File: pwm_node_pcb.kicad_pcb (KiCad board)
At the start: 4 copper layers, 40 x 35 mm, 42 parts, among them J1 CAN1, J2 TC2050-IDC-NL, J3 Battery, J5 Load Source, J6 5V Breakout, U1 LMR51430, U2 TJA1051T/3, U3 LD1117S33CTR, U4 STM32L432KCU, U5 TXB0104QPWRQ1, Y1 ECS-2520MV-080-BN

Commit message: Add version silkscreen and update pictures
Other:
- board text added: "Daniel Jeon pwm_node_pcb v0.1.0-alpha"
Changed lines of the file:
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@@
+		)
+	)
+	(gr_text "Daniel Jeon\npwm_node_pcb\nv0.1.0-alpha"
+		(at 165.5 97 0)
+		(layer "B.SilkS")
+		(effects
+			(font
+				(size 1 1)
+				(thickness 0.2)
+				(bold yes)
+			)
+			(justify top mirror)
 		)
 	)

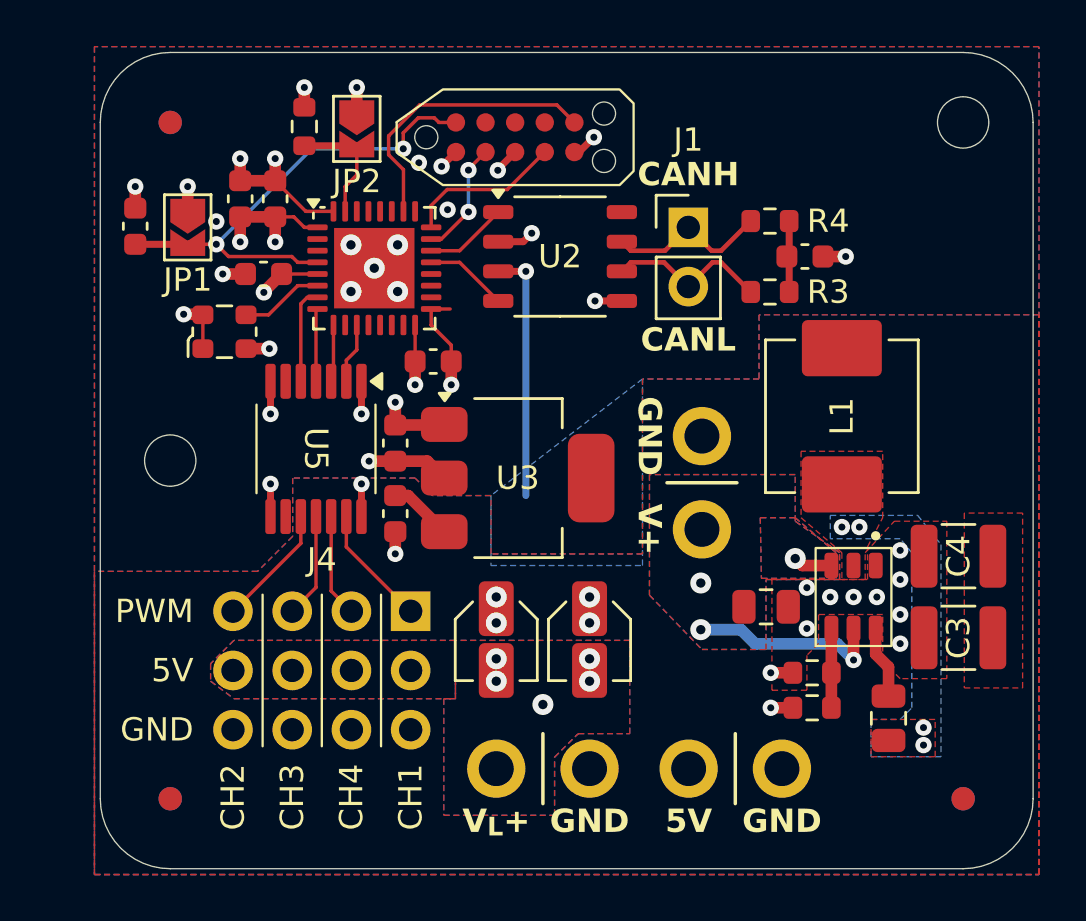
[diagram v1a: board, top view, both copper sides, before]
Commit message: Add minor decoupling caps, board cleanup
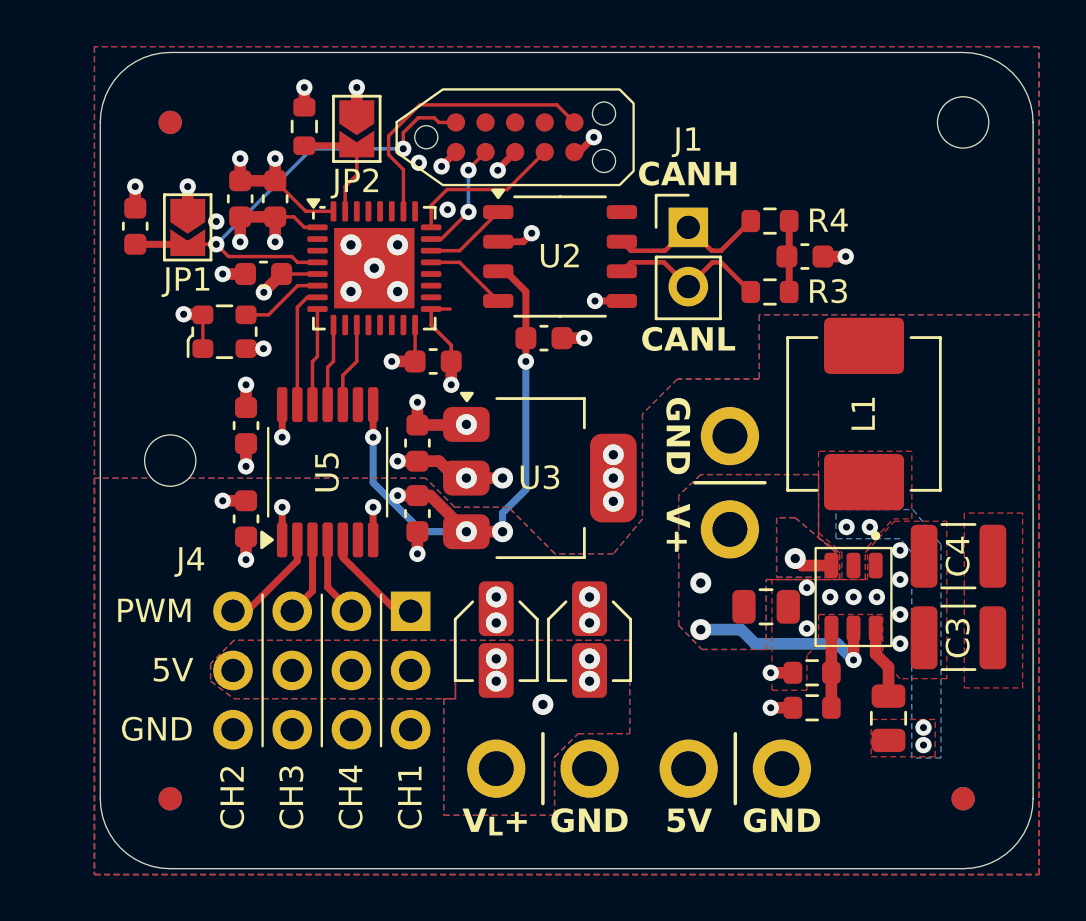
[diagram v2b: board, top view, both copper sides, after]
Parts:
- added C16: 100n, Capacitor_SMD:C_0603_1608Metric, F.Cu at (143.0, 115.8)
- added C17: 100n, Capacitor_SMD:C_0603_1608Metric, F.Cu at (143.0, 111.8)
- added C27: 100n, Capacitor_SMD:C_0603_1608Metric, F.Cu at (155.8, 108.0)
- moved J3 1.20 mm to (163.8, 114.2)
- moved U5 1.12 mm to (146.5, 113.8), turned to 90 degrees
- moved L1 0.96 mm to (169.5, 111.2)
- moved C5 0.95 mm to (150.3, 115.5)
- moved C6 0.95 mm to (150.3, 112.5)
- moved U3 0.95 mm to (155.6, 114.0)
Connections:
- U5 pad 1: +3V3 -> +5V
- U5 pad 10: /PWM2_{5V} -> /TIM1_CH1
- U5 pad 11: /PWM3_{5V} -> /TIM1_CH4
- U5 pad 12: /PWM4_{5V} -> /TIM1_CH3
- U5 pad 13: /PWM1_{5V} -> /TIM1_CH2
- U5 pad 14: +5V -> +3V3
- U5 pad 2: /TIM1_CH1 -> /PWM2_{5V}
- U5 pad 3: /TIM1_CH4 -> /PWM3_{5V}
- U5 pad 4: /TIM1_CH3 -> /PWM4_{5V}
- U5 pad 5: /TIM1_CH2 -> /PWM1_{5V}
- U5 pad 8: +3V3 -> +5V
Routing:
- net +5V: track 15.9 -> 29.4 mm, vias 3 -> 8
- net GND: track 24.9 -> 27.6 mm, vias 37 -> 41
- net /TIM1_CH1: track 2.60 -> 3.66 mm
- net /TIM1_CH2: track 4.15 -> 5.21 mm
- net /TIM1_CH3: track 3.13 -> 4.19 mm
- net /TIM1_CH4: track 2.45 -> 3.52 mm
- net /PWM3_{5V}: track 4.48 -> 3.42 mm
- net /PWM4_{5V}: track 4.42 -> 3.48 mm
- net +3V3: track 24.4 -> 25.2 mm, vias 11 -> 16
- net /PWM2_{5V}: track 5.27 -> 4.55 mm
- net /PWM1_{5V}: track 5.20 -> 4.62 mm

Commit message: Trace cleanup
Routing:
- net +5V: track 29.4 -> 25.8 mm
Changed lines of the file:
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@@
-	)
-	(segment
-		(start 154.885 103.865)
-		(end 153.815 103.865)
-		(width 0.3)
-		(layer "F.Cu")
-		(net 1)
 	)
 	(segment
@@
 	)
 	(segment
-		(start 155.25 103.5)
-		(end 154.885 103.865)
-		(width 0.3)
-		(layer "F.Cu")
-		(net 1)
-	)
-	(segment
 		(start 144.25 101.25)
 		(end 144.25 100.3)
@@
 	)
 	(segment
+		(start 155 103.865)
+		(end 153.815 103.865)
+		(width 0.3)
+		(layer "F.Cu")
+		(net 1)
+	)
+	(segment
 		(start 143.75 108.45)
 		(end 143 108.45)
@@
 	)
 	(via
-		(at 155.25 103.5)
+		(at 155 103.865)
 		(size 0.7)
 		(drill 0.3)
@@
 	)
 	(segment
+		(start 149.5 114.75)
+		(end 149 114.75)
+		(width 0.3)
+		(layer "B.Cu")
+		(net 2)
+	)
+	(segment
 		(start 154 115.5)
 		(end 154 116.3)
@@
 	)
 	(segment
-		(start 150.55 116.3)
-		(end 148.45 114.2)
-		(width 0.3)
-		(layer "B.Cu")
-		(net 2)
-	)
-	(segment
-		(start 152.45 116.3)
-		(end 150.55 116.3)
-		(width 0.3)
-		(layer "B.Cu")
-		(net 2)
-	)
-	(segment
 		(start 148.45 114.2)
 		(end 148.45 112.25)
+		(width 0.3)
+		(layer "B.Cu")
+		(net 2)
+	)
+	(segment
+		(start 149 114.75)
+		(end 148.45 114.2)
 		(width 0.3)
 		(layer "B.Cu")
@@
 		(polygon
 			(pts
-				(xy 152.5 104.25) (xy 152.5 104.75) (xy 153 104.75) (xy 152.965 104.25)
+				(xy 152.5 104.25) (xy 152.5 104.75) (xy 153 104.75) (xy 153 104.25)
 			)
 		)
@@
 		(polygon
 			(pts
-				(xy 151.98 123.46) (xy 151.48 123.46) (xy 151.48 128.46) (xy 156.23 128.46) (xy 156.23 125.964951)
+				(xy 151.98 123.46) (xy 151.48 123.46) (xy 151.48 128.71) (xy 156.23 128.71) (xy 156.23 125.964951)
 				(xy 157.245 124.96) (xy 159.455 124.96) (xy 159.455 120.96) (xy 151.98 120.96)
 			)

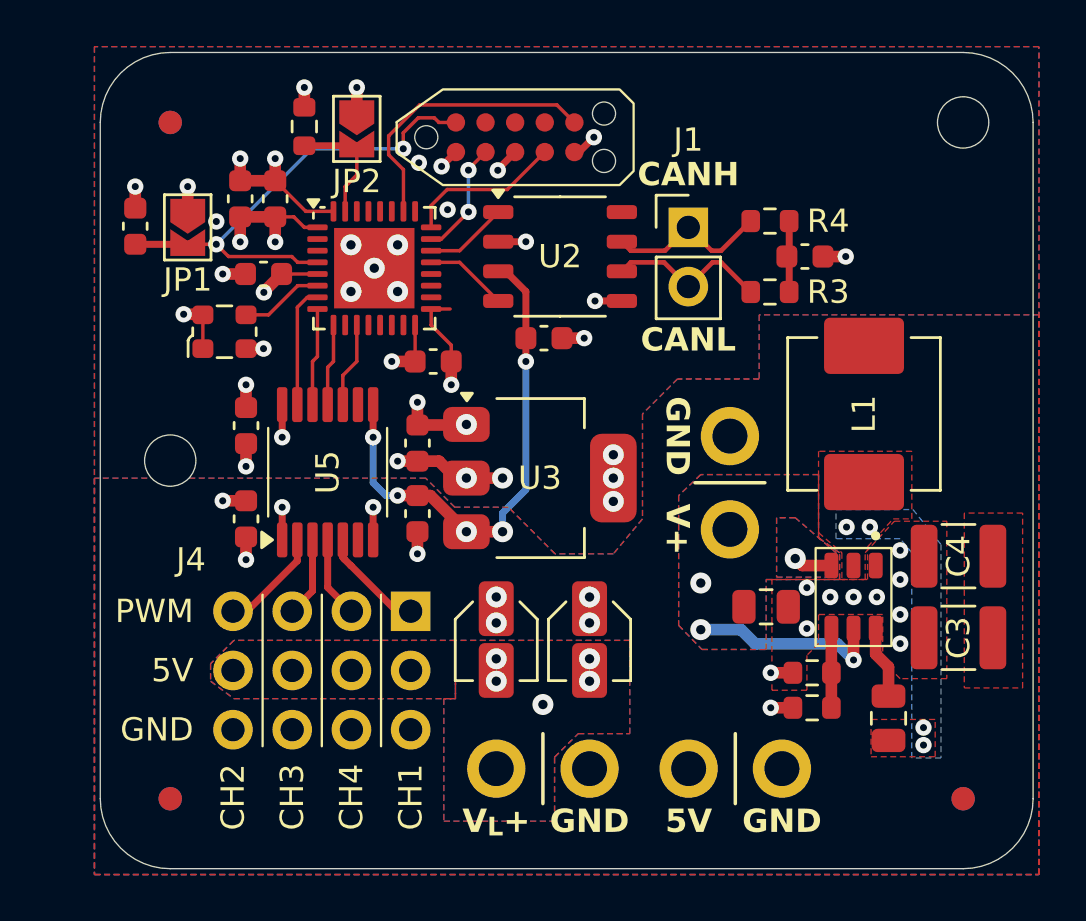
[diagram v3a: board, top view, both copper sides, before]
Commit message: Add TVS and schottky diodes
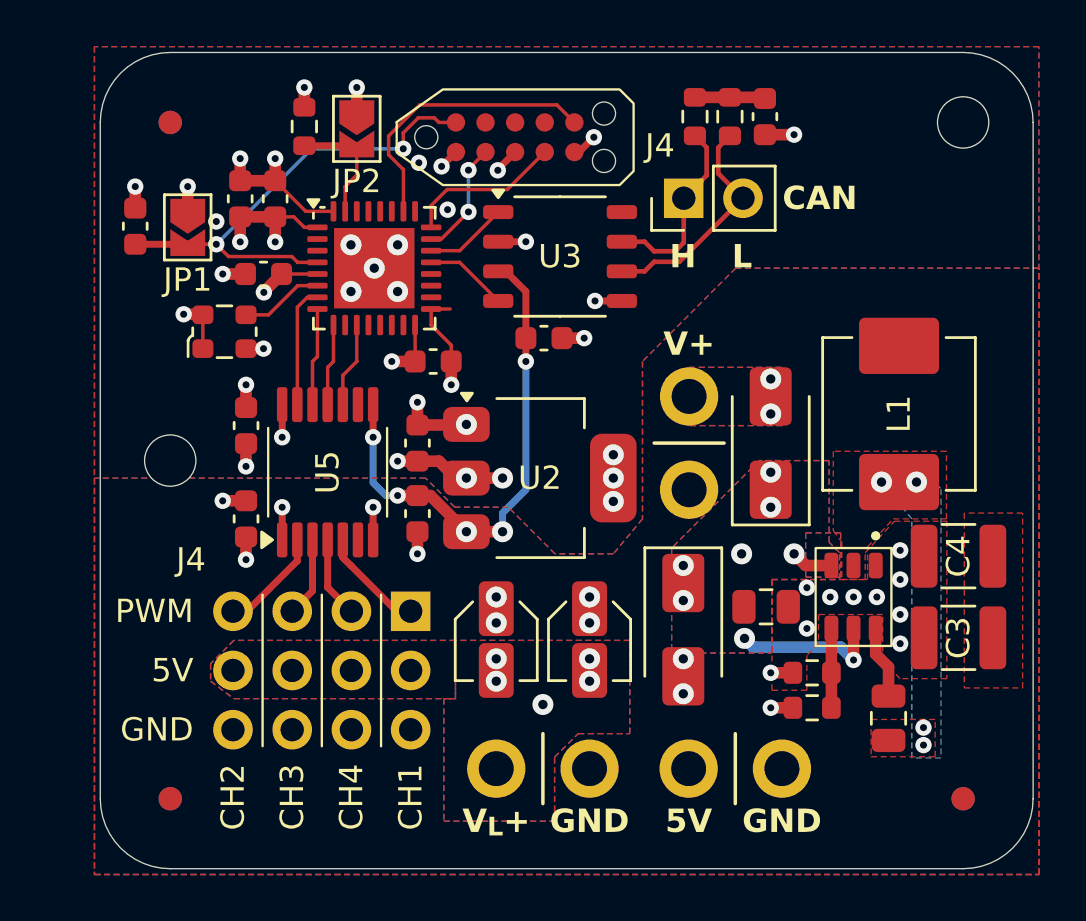
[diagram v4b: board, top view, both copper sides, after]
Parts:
- removed the J3 at (163.8, 114.2)
- added D1: Schottky, Diode_SMD:D_SMA, F.Cu at (165.5, 112.5)
- added D2: TVS, Diode_SMD:D_SMA, F.Cu at (161.8, 120.5)
- added J1: Battery, pwm_node_connectors:battery, B.Cu at (162.0, 112.5)
- moved R3 7.71 mm to (163.8, 98.5), turned to 90 degrees
- moved C13 6.24 mm to (165.2, 98.5), turned to -90 degrees
- moved R4 5.51 mm to (162.2, 98.5), turned to 90 degrees
- moved L1 1.50 mm to (171.0, 111.2)
- moved J4 1.27 mm to (161.8, 102.0), turned to 90 degrees
- renumbered C7 to C13, C16 to C14, C17 to C15, C15 to C16, C14 to C17, C27 to C7, J6 to J2, J2 to J3, J1 to J4, J4 to J6, U3 to U2, U2 to U3
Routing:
- net /CAN1-: track 7.07 -> 9.81 mm
- net +VSUPPLY: track 10.1 -> 8.22 mm, vias 4 -> 8
- net /CAN1+: track 7.04 -> 8.17 mm
- net GND: track 27.2 -> 27.5 mm, vias 41 -> 43
- net Net-(D1-A): vias 0 -> 2
- added copper zone on B.Cu, net Net-(D1-A)
- added copper zone on F.Cu, net Net-(D1-A)
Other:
- board text added: "CAN"
- board text added: "H"
- board text added: "L"
- board text removed: "CANH"
- board text removed: "CANL"

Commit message: Add GND plane stitching vias
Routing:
- net GND: vias 43 -> 65

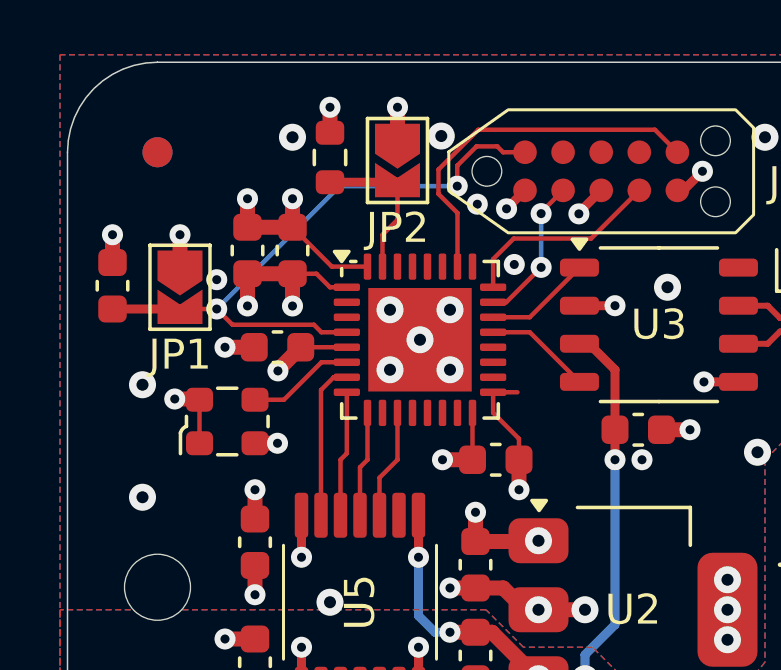
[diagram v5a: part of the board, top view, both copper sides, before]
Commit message: Add testpads/UART breakout
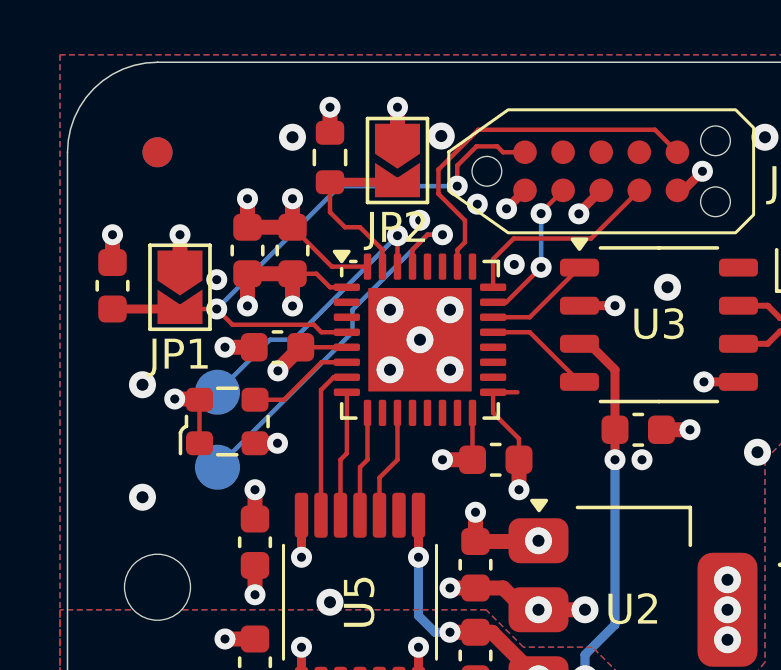
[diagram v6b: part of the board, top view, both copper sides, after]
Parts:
- added TP1: UART_RX, TestPoint:TestPoint_Pad_D1.5mm, B.Cu at (141.8, 109.2)
- added TP2: UART_TX, TestPoint:TestPoint_Pad_D1.5mm, B.Cu at (141.8, 106.8)
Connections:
- U4 pad 29: unconnected-(U4-PB6-Pad29) -> /USART1_RX
- U4 pad 30: unconnected-(U4-PB7-Pad30) -> /USART1_TX
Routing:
- net /USART1_RX: track 0.00 -> 12.9 mm, vias 0 -> 1
- net /USART1_TX: track 0.00 -> 9.19 mm, vias 0 -> 1
- net /BOOT0: track 5.27 -> 6.08 mm
- net GND: vias 65 -> 66
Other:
- board text added: "1"
- board text added: "2"
- board text added: "TP"

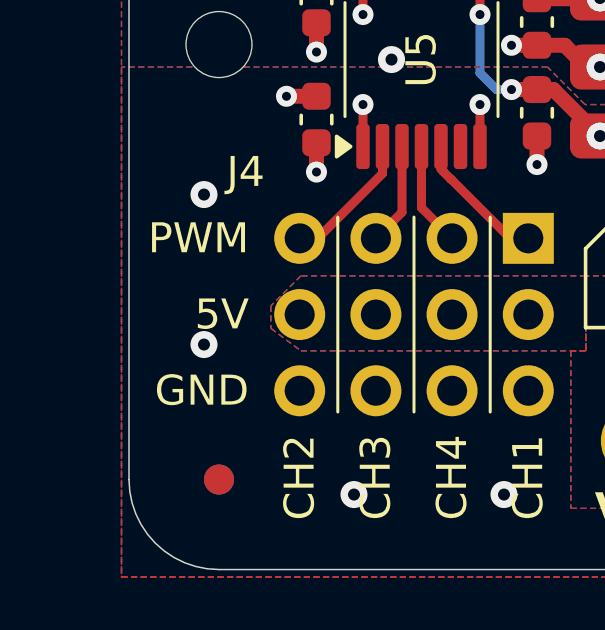
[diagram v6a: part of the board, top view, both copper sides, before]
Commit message: Fix silkscreen and load caps to 220uF
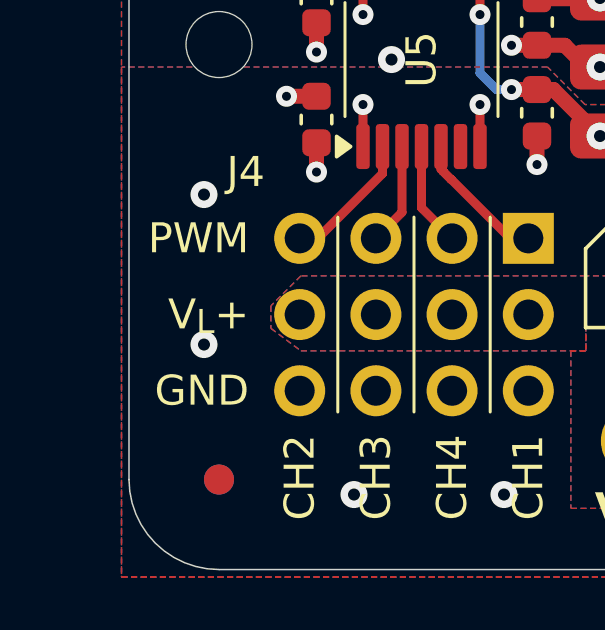
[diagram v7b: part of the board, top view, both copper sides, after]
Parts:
- C16, C17: value 2200u -> 220u
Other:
- board text added: "Daniel Jeon pwm_node_pcb v0.1.0"
- board text removed: "Daniel Jeon pwm_node_pcb v0.1.0-alpha"
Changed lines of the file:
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@@
 	(title_block
 		(title "pwm_node_pcb")
-		(rev "0.1.0-alpha")
+		(rev "0.1.0")
 		(company "Daniel Jeon")
 	)
@@
 			)
 		)
-		(property "Value" "2200u"
+		(property "Value" "220u"
 			(at 0 2.7 90)
 			(layer "F.Fab")
@@
 			)
 		)
-		(property "Value" "2200u"
+		(property "Value" "220u"
 			(at 0 2.7 90)
 			(layer "F.Fab")
@@
 		)
 	)
-	(gr_text "5V"
+	(gr_text "V_{L}+"
 		(at 140.75 122.25 0)
 		(layer "F.SilkS")
@@
 		)
 	)
-	(gr_text "5V"
+	(gr_text "V_{L}+"
 		(at 140.75 122.25 0)
 		(layer "B.SilkS")
@@
 		)
 	)
-	(gr_text "Daniel Jeon\npwm_node_pcb\nv0.1.0-alpha"
+	(gr_text "Daniel Jeon\npwm_node_pcb\nv0.1.0"
 		(at 170.5 107.25 0)
 		(layer "B.SilkS")

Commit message: Fix flipped UART breakout (TP) nets
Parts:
- TP1: value UART_RX -> UART_TX
- TP2: value UART_TX -> UART_RX
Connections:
- TP1 pad 1: /USART1_RX -> /USART1_TX
- TP2 pad 1: /USART1_TX -> /USART1_RX
- U4 pad 29: /USART1_RX -> /USART1_TX
- U4 pad 30: /USART1_TX -> /USART1_RX
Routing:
- net /USART1_TX: track 9.19 -> 12.9 mm
- net /USART1_RX: track 12.9 -> 9.19 mm
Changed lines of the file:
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@@
 			(layers "F.Cu" "F.Mask" "F.Paste")
 			(roundrect_rratio 0.25)
-			(net 25 "/USART1_RX")
+			(net 30 "/USART1_TX")
 			(pinfunction "PB6")
 			(pintype "bidirectional")
@@
 			(layers "F.Cu" "F.Mask" "F.Paste")
 			(roundrect_rratio 0.25)
-			(net 30 "/USART1_TX")
+			(net 25 "/USART1_RX")
 			(pinfunction "PB7")
 			(pintype "bidirectional")
@@
 			)
 		)
-		(property "Value" "UART_RX"
+		(property "Value" "UART_TX"
 			(at 0 -1.75 0)
 			(layer "B.Fab")
@@
 			(size 1.5 1.5)
 			(layers "B.Cu" "B.Mask")
-			(net 25 "/USART1_RX")
+			(net 30 "/USART1_TX")
 			(pinfunction "1")
 			(pintype "passive")
@@
 			)
 		)
-		(property "Value" "UART_TX"
+		(property "Value" "UART_RX"
 			(at 0 -1.75 0)
 			(layer "B.Fab")
@@
 			(size 1.5 1.5)
 			(layers "B.Cu" "B.Mask")
-			(net 30 "/USART1_TX")
+			(net 25 "/USART1_RX")
 			(pinfunction "1")
 			(pintype "passive")
@@
 	)
 	(segment
-		(start 148.75 101.5)
-		(end 148.25 102)
-		(width 0.15)
-		(layer "F.Cu")
-		(net 25)
-	)
-	(segment
-		(start 149.25 101.5)
-		(end 148.75 101.5)
-		(width 0.15)
-		(layer "F.Cu")
-		(net 25)
-	)
-	(segment
-		(start 148.25 102)
-		(end 148.25 102.5625)
+		(start 147.75 101.530811)
+		(end 147.75 102.5625)
 		(width 0.15)
 		(layer "F.Cu")
@@
 	)
 	(via
-		(at 149.25 101.5)
+		(at 147.75 101.530811)
 		(size 0.7)
 		(drill 0.3)
@@
 	)
 	(segment
-		(start 148.75 101.5)
-		(end 146.25 104)
+		(start 147.75 101.530811)
+		(end 144.280811 105)
 		(width 0.15)
 		(layer "B.Cu")
@@
 	)
 	(segment
-		(start 146.25 104.75)
-		(end 141.75 109.25)
+		(start 144.280811 105)
+		(end 143.5 105)
 		(width 0.15)
 		(layer "B.Cu")
@@
 	)
 	(segment
-		(start 149.25 101.5)
-		(end 148.75 101.5)
+		(start 143.5 105)
+		(end 141.75 106.75)
 		(width 0.15)
 		(layer "B.Cu")
@@
 	)
 	(segment
-		(start 146.25 104)
-		(end 146.25 104.75)
+		(start 148.75 101.5)
+		(end 148.25 102)
 		(width 0.15)
-		(layer "B.Cu")
-		(net 25)
+		(layer "F.Cu")
+		(net 30)
 	)
 	(segment
-		(start 147.75 101.530811)
-		(end 147.75 102.5625)
+		(start 149.25 101.5)
+		(end 148.75 101.5)
+		(width 0.15)
+		(layer "F.Cu")
+		(net 30)
+	)
+	(segment
+		(start 148.25 102)
+		(end 148.25 102.5625)
 		(width 0.15)
 		(layer "F.Cu")
@@
 	)
 	(via
-		(at 147.75 101.530811)
+		(at 149.25 101.5)
 		(size 0.7)
 		(drill 0.3)
@@
 	)
 	(segment
-		(start 147.75 101.530811)
-		(end 144.280811 105)
+		(start 148.75 101.5)
+		(end 146.25 104)
 		(width 0.15)
 		(layer "B.Cu")
@@
 	)
 	(segment
-		(start 144.280811 105)
-		(end 143.5 105)
+		(start 146.25 104.75)
+		(end 141.75 109.25)
 		(width 0.15)
 		(layer "B.Cu")
@@
 	)
 	(segment
-		(start 143.5 105)
-		(end 141.75 106.75)
+		(start 149.25 101.5)
+		(end 148.75 101.5)
+		(width 0.15)
+		(layer "B.Cu")
+		(net 30)
+	)
+	(segment
+		(start 146.25 104)
+		(end 146.25 104.75)
 		(width 0.15)
 		(layer "B.Cu")
